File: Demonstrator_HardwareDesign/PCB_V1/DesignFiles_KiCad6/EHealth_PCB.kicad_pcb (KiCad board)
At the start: 2 copper layers, 50 x 50 mm, 24 parts

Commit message: aangepaste pcb layout
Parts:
- removed AnalogSensors: Conn_01x05, Connector_PinHeader_2.54mm:PinHeader_1x05_P2.54mm_Vertical
- removed R10, R11, R12, R5, R6, R7, R8, R9: R, Resistor_SMD:R_0805_2012Metric_Pad1.20x1.40mm_HandSolder
- added J1: Conn_01x06, Connector_PinHeader_2.54mm:PinHeader_2x04_P2.54mm_Vertical, F.Cu at (215.2, 92.2)
- added R16: R, Resistor_SMD:R_0805_2012Metric_Pad1.20x1.40mm_HandSolder, F.Cu at (208.0, 99.3)
- added R17: R, Resistor_SMD:R_0805_2012Metric_Pad1.20x1.40mm_HandSolder, F.Cu at (208.1, 94.2)
- added R21: R, Resistor_SMD:R_0805_2012Metric_Pad1.20x1.40mm_HandSolder, F.Cu at (210.0, 97.0)
- added R22: R, Resistor_SMD:R_0805_2012Metric_Pad1.20x1.40mm_HandSolder, F.Cu at (210.1, 91.9)
- J3-MagneticInterconnect1: renamed from MagneticInterconnect; footprint Connector_JST:JST_VH_B8P-VH-B_1x08_P3.96mm_Vertical -> Connector_JST:JST_VH_B4P-VH-B_1x04_P3.96mm_Vertical
- J4-OffTheShelf-Digital1: renamed from Digital; footprint Connector_PinSocket_2.54mm:PinSocket_2x06_P2.54mm_Vertical -> Connector_PinSocket_2.54mm:PinSocket_2x04_P2.54mm_Vertical
- moved R1 10.8 mm to (193.0, 103.8)
- moved R18 8.32 mm to (225.5, 102.2), turned to 0 degrees
- moved R20 8.32 mm to (225.5, 91.9), turned to 0 degrees
- moved R19 8.31 mm to (225.5, 97.0), turned to 0 degrees
- moved R14 7.96 mm to (223.5, 99.3)
- moved R13 7.95 mm to (223.5, 104.3)
- moved R15 7.95 mm to (223.5, 94.2)
- renumbered Power to J5-Power1, R16 to R18, R17 to R19, R18 to R20
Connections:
- LOLIN_C3_PICO1 pad 15: Net-(J1-AnalogSensors1-Pin_5) -> unconnected-(LOLIN_C3_PICO1-5_-_A5-Pad15)
- R13 pad 1: Net-(J1-AnalogSensors1-Pin_5) -> /SPI_MOSI
- R18 pad 1: Net-(J1-AnalogSensors1-Pin_5) -> /SPI_MOSI
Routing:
- net /SPI_CS: track 73.5 -> 0.00 mm, vias 2 -> 0
- net /SPI_MISO: track 82.2 -> 18.5 mm, vias 1 -> 0
- net Net-(J1-AnalogSensors1-Pin_5): track 34.4 -> 0.00 mm
- net +3.3V: track 140.5 -> 172.1 mm, vias 3 -> 6
- net /SPI_SCK: track 68.1 -> 40.6 mm, vias 1 -> 0
- net /SPI_MOSI: track 67.0 -> 44.6 mm
- net GND: track 47.4 -> 27.6 mm, vias 10 -> 8
- net Net-(J4-OffTheShelf-Digital1-Pin_5): track 23.5 -> 12.6 mm
- net /GPIO21_TX: track 55.4 -> 49.9 mm
- net /GPIO20_RX: track 52.1 -> 47.2 mm
- net /GPIO4_LED: track 66.5 -> 62.2 mm, vias 2 -> 0
- net Net-(J1-Pin_4): track 47.2 -> 43.6 mm
- net Net-(J1-Pin_5): track 51.8 -> 52.6 mm, vias 0 -> 2
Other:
- outline, holes or cut-outs redrawn
- board text added: "GPIO0"
- board text added: "GPIO1"
- board text added: "GPIO2"
- board text added: "IMO-IMOMEC"
- board text removed: "CS"
- board text removed: "CS SCK"
- board text removed: "GPIO5"
- board text removed: "MISO"
- board text removed: "MOSI"
- board text removed: "MOSI MISO"
- board text removed: "Optional"
- board text removed: "SCK"
- board text removed: "SPI P_Up/Down"

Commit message: aangepaste layout
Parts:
- removed R1, R18, R19, R20, R21, R22: R, Resistor_SMD:R_0805_2012Metric_Pad1.20x1.40mm_HandSolder
- J1: footprint Connector_PinHeader_2.54mm:PinHeader_2x04_P2.54mm_Vertical -> Connector_PinHeader_2.54mm:PinHeader_2x05_P2.54mm_Vertical
- moved J4-OffTheShelf-Digital1 25.3 mm to (183.8, 76.2), turned to 0 degrees
- moved J1 15.4 mm to (226.3, 103.0), turned to 180 degrees
- moved R13 13.1 mm to (216.5, 93.2)
- moved R17 11.8 mm to (216.5, 102.5)
- moved R16 8.52 mm to (216.5, 100.1)
- moved R15 7.90 mm to (216.5, 97.8)
- moved R14 7.89 mm to (216.5, 95.6)
- renumbered J3-MagneticInterconnect1 to MagneticInterconnect1
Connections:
- J1 pad 1: +3.3V -> GND
- J1 pad 2: GND -> Net-(J1-Pin_2)
- J1 pad 3: /SPI_SCK -> GND
- J1 pad 5: Net-(J1-Pin_5) -> GND
- J1 pad 6: /SPI_MOSI -> Net-(J1-Pin_6)
- J1 pad 7: /SPI_MISO -> GND
- J1 pad 8: GND -> Net-(J1-Pin_8)
- J4-OffTheShelf-Digital1 pad 5: Net-(J4-OffTheShelf-Digital1-Pin_5) -> /SPI_CS
- LOLIN_C3_PICO1 pad 10: Net-(J1-Pin_5) -> Net-(J1-Pin_8)
- LOLIN_C3_PICO1 pad 11: Net-(J1-Pin_4) -> Net-(J1-Pin_6)
- LOLIN_C3_PICO1 pad 12: /SPI_SCK -> Net-(J1-Pin_4)
- LOLIN_C3_PICO1 pad 13: /SPI_MISO -> Net-(J1-Pin_2)
- LOLIN_C3_PICO1 pad 14: /SPI_MOSI -> Net-(J1-Pin_10)
- MagneticInterconnect1 pad 1: +3.3V -> Vdd
- R13 pad 1: /SPI_MOSI -> Net-(J1-Pin_10)
- R14 pad 1: Net-(J1-Pin_5) -> Net-(J1-Pin_8)
- R15 pad 1: Net-(J1-Pin_4) -> Net-(J1-Pin_6)
- R16 pad 1: /SPI_SCK -> Net-(J1-Pin_4)
- R17 pad 1: /SPI_MISO -> Net-(J1-Pin_2)
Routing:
- net Net-(J1-Pin_5): track 52.6 -> 0.00 mm, vias 2 -> 0
- net Net-(J1-Pin_8): track 0.00 -> 52.3 mm, vias 0 -> 1
- net +3.3V: track 172.1 -> 120.3 mm, vias 6 -> 2
- net /SPI_CS: track 0.00 -> 49.1 mm, vias 0 -> 2
- net Net-(J1-Pin_6): track 0.00 -> 47.1 mm, vias 0 -> 1
- net /SPI_MOSI: track 44.6 -> 0.00 mm, vias 1 -> 0
- net /SPI_SCK: track 40.6 -> 0.00 mm
- net Net-(J1-Pin_2): track 0.00 -> 37.7 mm
- net /SCL: track 79.2 -> 54.2 mm
- net Net-(J1-Pin_10): track 0.00 -> 22.2 mm, vias 0 -> 1
- net /SPI_MISO: track 18.5 -> 0.00 mm
- net Net-(J4-OffTheShelf-Digital1-Pin_5): track 12.6 -> 0.00 mm
- net GND: track 27.6 -> 16.4 mm, vias 8 -> 2
- net /GPIO20_RX: track 47.2 -> 41.0 mm
- net /GPIO21_TX: track 49.9 -> 46.3 mm, vias 0 -> 2
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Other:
- outline, holes or cut-outs redrawn
- board text added: "Analog sensors"
- board text added: "Buck Convertor"
- board text removed: "Analog sensors: Mandatory Resistor deviders"
- board text removed: "Connect sensor to 3.3V or GND externally!"
- board text removed: "IMO-IMOMEC"
- board text removed: "Optional 0805 to ground"

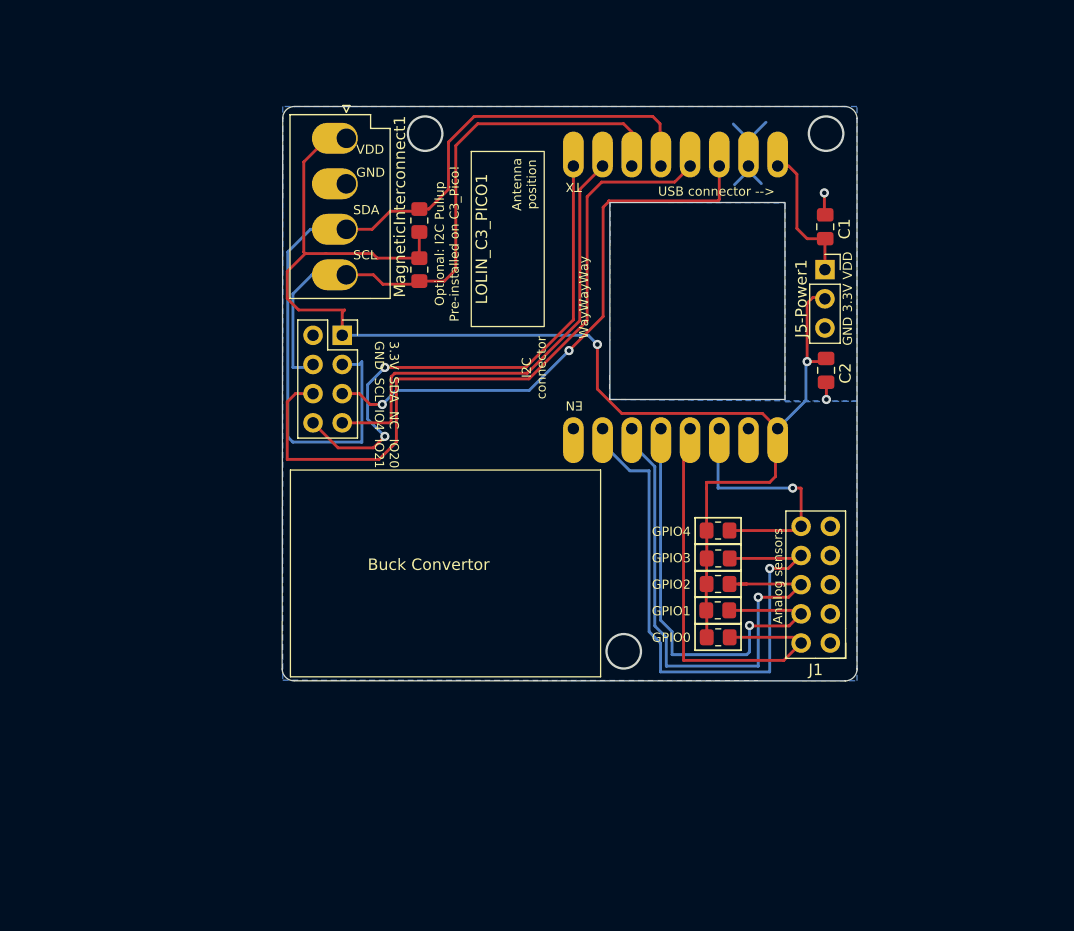
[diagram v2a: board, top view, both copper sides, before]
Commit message: layout met buck en mult chip
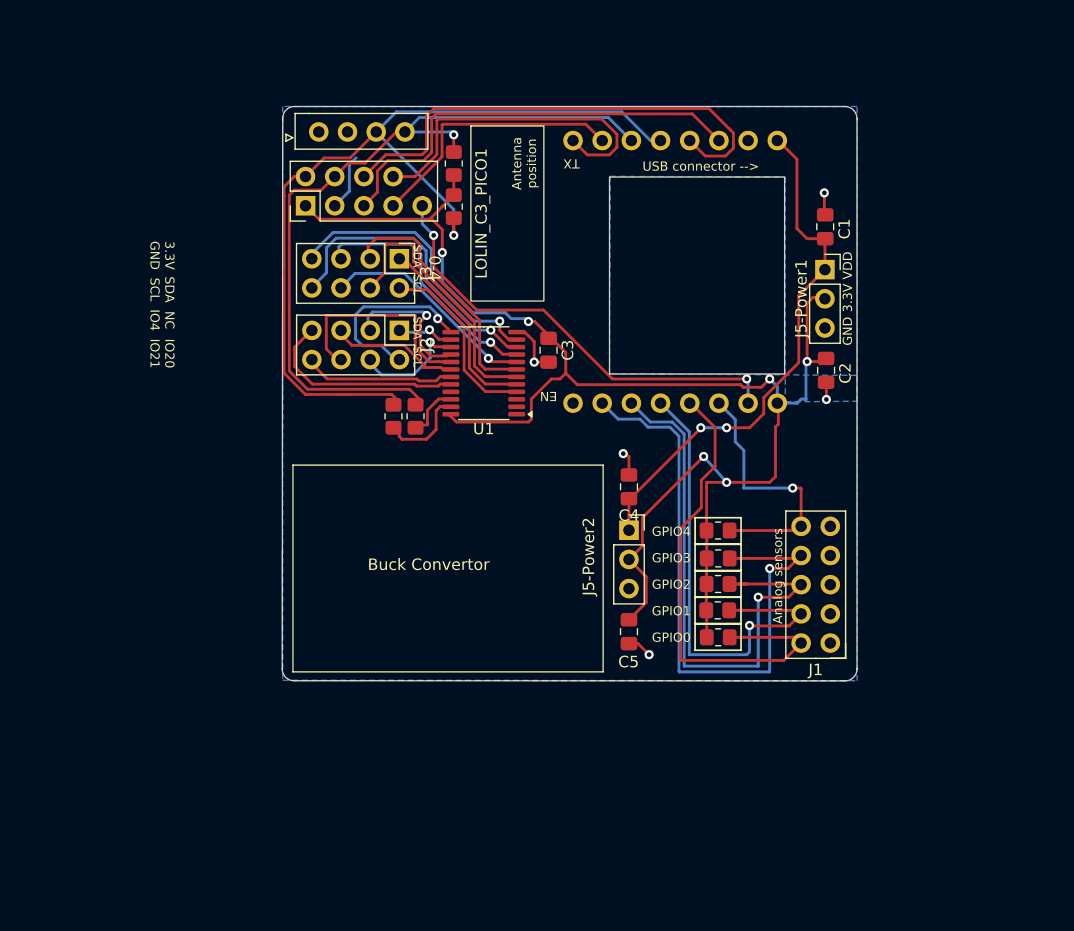
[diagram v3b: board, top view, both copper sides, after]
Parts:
- added C3: C_Small, Capacitor_SMD:C_0805_2012Metric_Pad1.18x1.45mm_HandSolder, F.Cu at (201.8, 77.5)
- added C4: C_Small, Capacitor_SMD:C_0805_2012Metric_Pad1.18x1.45mm_HandSolder, F.Cu at (208.8, 89.4)
- added C5: C_Small, Capacitor_SMD:C_0805_2012Metric_Pad1.18x1.45mm_HandSolder, F.Cu at (208.8, 102.0)
- added J2: Conn_01x06, Connector_PinHeader_2.54mm:PinHeader_2x04_P2.54mm_Vertical, F.Cu at (188.8, 75.8)
- added J3: Conn_01x06, Connector_PinHeader_2.54mm:PinHeader_2x04_P2.54mm_Vertical, F.Cu at (188.8, 69.5)
- added J5-Power2: Conn_01x03, Connector_PinSocket_2.54mm:PinSocket_1x03_P2.54mm_Vertical, F.Cu at (208.8, 93.2)
- added R1: R, Resistor_SMD:R_0805_2012Metric_Pad1.20x1.40mm_HandSolder, F.Cu at (190.2, 83.2)
- added R4: R, Resistor_SMD:R_0805_2012Metric_Pad1.20x1.40mm_HandSolder, F.Cu at (188.2, 83.2)
- added U1: TCA9548APWR, Package_SO:TSSOP-24_4.4x7.8mm_P0.65mm, F.Cu at (196.1, 79.5)
- J4-OffTheShelf-Digital1: footprint Connector_PinSocket_2.54mm:PinSocket_2x04_P2.54mm_Vertical -> Connector_PinHeader_2.54mm:PinHeader_2x05_P2.54mm_Vertical
- moved J4-OffTheShelf-Digital1 11.7 mm to (180.6, 64.9), turned to 90 degrees
- moved R3 9.71 mm to (193.5, 61.2), turned to -90 degrees
- moved R2 3.23 mm to (193.5, 65.0), turned to 90 degrees
- moved J3-MagneticInterconnect1 2.40 mm to (181.8, 59.0), turned to 0 degrees
- moved LOLIN_C3_PICO1 2.22 mm to (214.0, 69.4)
- renumbered MagneticInterconnect1 to J3-MagneticInterconnect1
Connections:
- J4-OffTheShelf-Digital1 pad 2: GND -> /SDA
- J4-OffTheShelf-Digital1 pad 3: /SDA -> GND
- LOLIN_C3_PICO1 pad 15: unconnected-(LOLIN_C3_PICO1-5_-_A5-Pad15) -> /A5
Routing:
- net /A5: track 0.00 -> 39.2 mm, vias 0 -> 2
- net VDD: track 12.2 -> 46.1 mm, vias 0 -> 2
- net Net-(J3-Pin_8): track 0.00 -> 26.4 mm, vias 0 -> 1
- net Net-(J3-Pin_7): track 0.00 -> 24.9 mm, vias 0 -> 1
- net Net-(J3-Pin_4): track 0.00 -> 23.6 mm
- net Net-(J3-Pin_3): track 0.00 -> 22.0 mm
- net Net-(J3-Pin_5): track 0.00 -> 22.0 mm, vias 0 -> 1
- net /GPIO4_LED: track 62.8 -> 43.2 mm
- net Net-(J3-Pin_6): track 0.00 -> 19.2 mm, vias 0 -> 1
- net Net-(J2-Pin_6): track 0.00 -> 18.4 mm
- net Net-(J2-Pin_7): track 0.00 -> 17.7 mm
- net Net-(J3-Pin_1): track 0.00 -> 16.8 mm
- net /GPIO21_TX: track 46.3 -> 29.6 mm, vias 2 -> 0
- net /GPIO20_RX: track 41.0 -> 24.3 mm
- net Net-(J2-Pin_2): track 0.00 -> 16.1 mm, vias 0 -> 1
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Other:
- outline, holes or cut-outs redrawn
- board text added: "0-4"
- board text removed: "I2C connector"
- board text removed: "Optional: I2C Pullup Pre-installed on C3_Pico!"
- board text removed: "WayWayWay"

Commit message: schema met mult chip en buck convertor
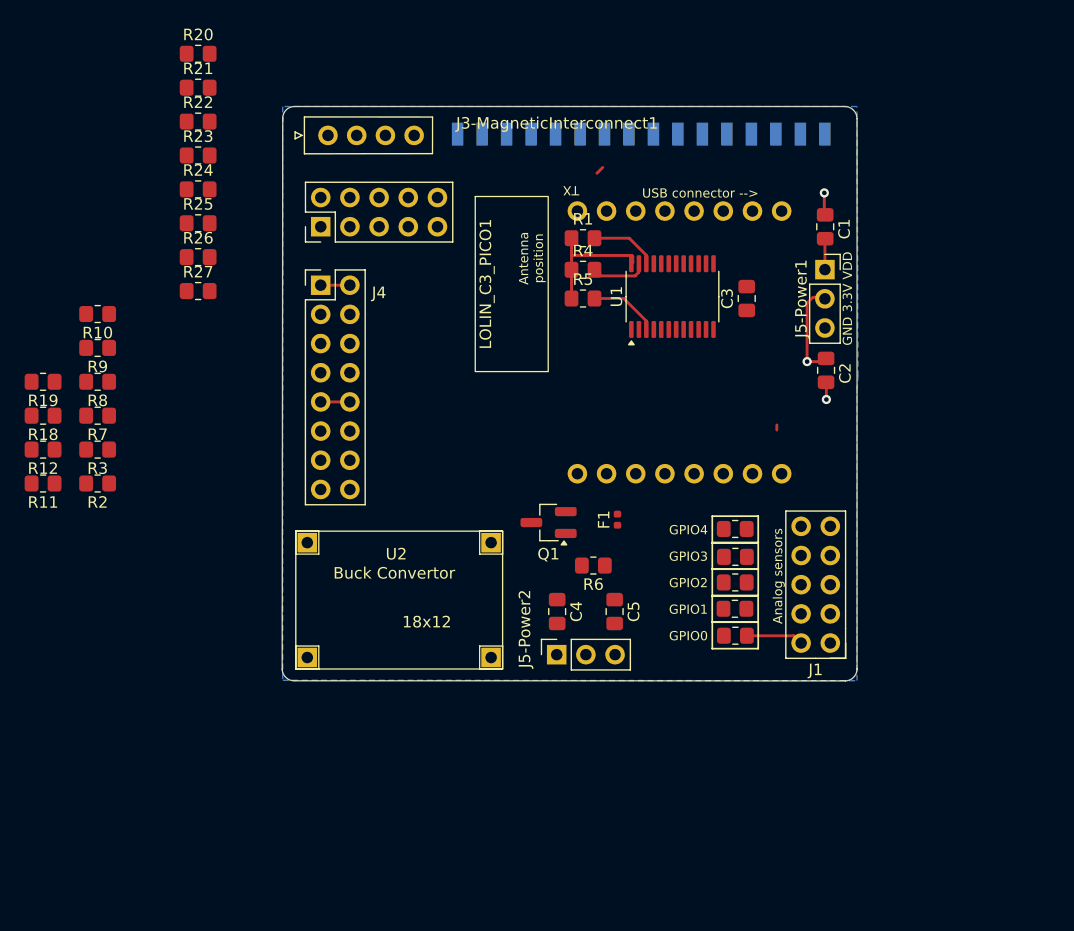
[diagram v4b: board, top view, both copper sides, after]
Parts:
- removed J3: Conn_01x06, Connector_PinHeader_2.54mm:PinHeader_2x04_P2.54mm_Vertical
- added F1: Fuse, Fuse:Fuse_0402_1005Metric, F.Cu at (207.8, 92.2)
- added J4: Conn_01x06, Connector_PinHeader_2.54mm:PinHeader_2x08_P2.54mm_Vertical, F.Cu at (181.9, 71.8)
- added Q1: PMOS, Package_TO_SOT_SMD:SOT-23_Handsoldering, F.Cu at (201.8, 92.5)
- added R10: R, Resistor_SMD:R_0805_2012Metric_Pad1.20x1.40mm_HandSolder, F.Cu at (162.5, 74.3)
- added R11: R, Resistor_SMD:R_0805_2012Metric_Pad1.20x1.40mm_HandSolder, F.Cu at (157.8, 89.1)
- added R12: R, Resistor_SMD:R_0805_2012Metric_Pad1.20x1.40mm_HandSolder, F.Cu at (157.8, 86.2)
- added R18: R, Resistor_SMD:R_0805_2012Metric_Pad1.20x1.40mm_HandSolder, F.Cu at (157.8, 83.2)
- added R19: R, Resistor_SMD:R_0805_2012Metric_Pad1.20x1.40mm_HandSolder, F.Cu at (157.8, 80.2)
- added R20: R, Resistor_SMD:R_0805_2012Metric_Pad1.20x1.40mm_HandSolder, F.Cu at (171.2, 51.7)
- added R21: R, Resistor_SMD:R_0805_2012Metric_Pad1.20x1.40mm_HandSolder, F.Cu at (171.2, 54.6)
- added R22: R, Resistor_SMD:R_0805_2012Metric_Pad1.20x1.40mm_HandSolder, F.Cu at (171.2, 57.6)
- added R23: R, Resistor_SMD:R_0805_2012Metric_Pad1.20x1.40mm_HandSolder, F.Cu at (171.2, 60.5)
- added R24: R, Resistor_SMD:R_0805_2012Metric_Pad1.20x1.40mm_HandSolder, F.Cu at (171.2, 63.5)
- added R25: R, Resistor_SMD:R_0805_2012Metric_Pad1.20x1.40mm_HandSolder, F.Cu at (171.2, 66.5)
- added R26: R, Resistor_SMD:R_0805_2012Metric_Pad1.20x1.40mm_HandSolder, F.Cu at (171.2, 69.4)
- added R27: R, Resistor_SMD:R_0805_2012Metric_Pad1.20x1.40mm_HandSolder, F.Cu at (171.2, 72.3)
- added R5: R, Resistor_SMD:R_0805_2012Metric_Pad1.20x1.40mm_HandSolder, F.Cu at (204.8, 73.0)
- added R6: R, Resistor_SMD:R_0805_2012Metric_Pad1.20x1.40mm_HandSolder, F.Cu at (205.7, 96.2)
- added R7: R, Resistor_SMD:R_0805_2012Metric_Pad1.20x1.40mm_HandSolder, F.Cu at (162.5, 83.2)
- added R8: R, Resistor_SMD:R_0805_2012Metric_Pad1.20x1.40mm_HandSolder, F.Cu at (162.5, 80.2)
- added R9: R, Resistor_SMD:R_0805_2012Metric_Pad1.20x1.40mm_HandSolder, F.Cu at (162.5, 77.3)
- added U2: DEBO DCDC DOWN 4, DEBO DCDC DOWN 4:DEBO DCDC DOWN 4, F.Cu at (188.8, 97.2)
- J2: footprint Connector_PinHeader_2.54mm:PinHeader_2x04_P2.54mm_Vertical -> Connector_PinHeader_2.54mm:PinHeader_1x16_P2.54mm_Vertical; moved to B.Cu
- moved J2 45.4 mm to (230.8, 58.7), turned to 90 degrees
- moved R3 39.8 mm to (162.5, 86.2), turned to 180 degrees
- moved R2 39.3 mm to (162.5, 89.1), turned to 180 degrees
- moved R1 21.3 mm to (204.8, 67.8), turned to 0 degrees
- moved R4 20.9 mm to (204.8, 70.5), turned to 0 degrees
- moved C3 17.8 mm to (219.0, 73.0), turned to 90 degrees
- moved U1 17.7 mm to (212.5, 72.8), turned to 90 degrees
- moved C4 12.5 mm to (202.5, 100.2)
- moved J5-Power2 12.5 mm to (202.5, 104.0), turned to 90 degrees
- moved LOLIN_C3_PICO1 6.15 mm to (214.4, 75.5)
- moved J4-OffTheShelf-Digital1 2.25 mm to (181.9, 66.8)
- moved C5 2.15 mm to (207.5, 100.2), turned to -90 degrees
- moved R13 1.50 mm to (218.0, 93.1)
- moved R14 1.50 mm to (218.0, 95.5)
- moved R15 1.50 mm to (218.0, 97.7)
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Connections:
- J2 pad 1: Net-(J2-Pin_1) -> +3.3V
- J2 pad 2: Net-(J2-Pin_2) -> +3.3V
- J2 pad 3: Net-(J2-Pin_3) -> GND
- J2 pad 4: Net-(J2-Pin_4) -> GND
- J3-MagneticInterconnect1 pad 1: Vdd -> VDD_12V
- J3-MagneticInterconnect1 pad 2: GND -> GND_12V
- J4-OffTheShelf-Digital1 pad 1: +3.3V -> /A5
- J4-OffTheShelf-Digital1 pad 2: /SDA -> +3.3V
- J4-OffTheShelf-Digital1 pad 3: GND -> /SPI_CS
- J4-OffTheShelf-Digital1 pad 4: /SCL -> GND
- J4-OffTheShelf-Digital1 pad 5: /SPI_CS -> /GPIO4_LED
- J4-OffTheShelf-Digital1 pad 6: /GPIO4_LED -> /SDA
- J4-OffTheShelf-Digital1 pad 8: /GPIO21_TX -> /SCL
- J4-OffTheShelf-Digital1 pad 9: /A5 -> /GPIO21_TX
- R1 pad 1: Net-(U1-SCL) -> +3.3V
- R4 pad 1: /SDA -> +3.3V
- R4 pad 2: Net-(U1-SDA) -> /SDA
- U1 pad 13: Net-(J2-Pin_2) -> Net-(J2-Pin_7)
- U1 pad 14: Net-(J2-Pin_1) -> Net-(J2-Pin_5)
- U1 pad 15: Net-(J2-Pin_4) -> Net-(J2-Pin_8)
- U1 pad 16: Net-(J2-Pin_3) -> Net-(J2-Pin_6)
- U1 pad 17: Net-(J2-Pin_6) -> Net-(J2-Pin_15)
- U1 pad 18: Net-(J2-Pin_5) -> Net-(J2-Pin_13)
- U1 pad 19: Net-(J2-Pin_8) -> Net-(J2-Pin_16)
- U1 pad 20: Net-(J2-Pin_7) -> Net-(J2-Pin_14)
- U1 pad 22: Net-(U1-SCL) -> /SCL
- U1 pad 23: Net-(U1-SDA) -> /SDA
- U1 pad 3: unconnected-(U1-~{RESET}-Pad3) -> Net-(U1-~{RESET})
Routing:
- net +3.3V: track 134.4 -> 25.6 mm, vias 6 -> 1
- net /SDA: track 78.1 -> 4.95 mm, vias 1 -> 0
- net /SCL: track 67.3 -> 5.86 mm, vias 1 -> 0
- net Net-(J1-Pin_8): track 54.8 -> 0.00 mm, vias 1 -> 0
- net Net-(J1-Pin_6): track 49.5 -> 0.09 mm, vias 1 -> 0
- net VDD: track 46.1 -> 2.70 mm, vias 2 -> 0
- net /GPIO4_LED: track 43.2 -> 0.00 mm
- net Net-(J1-Pin_4): track 42.1 -> 0.43 mm, vias 1 -> 0
- net /A5: track 39.2 -> 0.00 mm, vias 2 -> 0
- net /SPI_CS: track 38.0 -> 0.00 mm
- net Net-(J1-Pin_2): track 42.0 -> 4.99 mm
- net /GPIO21_TX: track 29.6 -> 0.00 mm
- net Net-(J4-Pin_16): track 26.4 -> 0.00 mm, vias 1 -> 0
- net Net-(J4-Pin_14): track 24.9 -> 0.00 mm, vias 1 -> 0
- net /GPIO20_RX: track 24.3 -> 0.72 mm
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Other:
- board text added: "18x12"
- board text removed: "0-4"
- board text removed: "3.3V GND"
- board text removed: "EN"
- board text removed: "IO20 IO21"
- board text removed: "NC IO4"
- board text removed: "SCL"
- board text removed: "SDA"
- board text removed: "SDA SCL"

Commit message: up to date
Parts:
- moved R27 52.2 mm to (222.1, 84.0), turned to 90 degrees
- moved R26 50.1 mm to (219.2, 84.0), turned to 90 degrees
- moved R25 48.3 mm to (216.2, 84.0), turned to 90 degrees
- moved R24 46.7 mm to (213.2, 84.0), turned to 90 degrees
- moved R23 45.6 mm to (210.3, 84.0), turned to 90 degrees
- moved R22 44.7 mm to (207.3, 84.0), turned to 90 degrees
- moved R21 44.3 mm to (204.4, 84.0), turned to 90 degrees
- moved R20 44.2 mm to (201.4, 84.0), turned to 90 degrees
- moved R11 36.3 mm to (194.0, 89.7)
- moved R12 36.3 mm to (194.0, 86.7)
- moved R18 36.3 mm to (194.0, 83.8)
- moved R19 36.3 mm to (194.0, 80.8)
- moved R10 26.8 mm to (189.2, 74.9)
- moved R2 26.8 mm to (189.2, 89.7)
- moved R3 26.8 mm to (189.2, 86.7)
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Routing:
- net +3.3V: track 25.6 -> 14.3 mm
- net Net-(U1-~{RESET}): track 6.06 -> 0.00 mm
- net /SCL: track 5.86 -> 0.00 mm
- net Net-(J1-Pin_2): track 4.99 -> 0.00 mm
- net /SDA: track 4.95 -> 0.00 mm
- net /GPIO20_RX: track 0.72 -> 0.00 mm

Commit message: up to date
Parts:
- F1: footprint Fuse:Fuse_0402_1005Metric -> Fuse:Fuse_0805_2012Metric_Pad1.15x1.40mm_HandSolder
- Q1: footprint Package_TO_SOT_SMD:SOT-23_Handsoldering -> Package_SO:Infineon_PG-DSO-8-27_3.9x4.9mm_EP2.65x3mm
- moved R19 29.0 mm to (222.8, 84.5), turned to 90 degrees
- moved R18 26.5 mm to (220.4, 84.5), turned to 90 degrees
- moved R2 25.0 mm to (213.8, 84.5), turned to 90 degrees
- moved R12 24.3 mm to (218.2, 84.5), turned to 90 degrees
- moved R11 22.6 mm to (216.0, 84.5), turned to 90 degrees
- moved R3 22.4 mm to (211.5, 84.5), turned to -90 degrees
- moved R7 20.0 mm to (209.2, 84.5), turned to -90 degrees
- moved R8 18.1 mm to (207.0, 84.5), turned to -90 degrees
- moved R9 16.9 mm to (204.8, 84.5), turned to -90 degrees
- moved R10 16.4 mm to (202.5, 84.5), turned to -90 degrees
- moved R20 15.4 mm to (207.2, 69.8)
- moved F1 15.3 mm to (193.2, 87.2), turned to -90 degrees
- moved R21 15.1 mm to (209.2, 69.8)
- moved R22 14.8 mm to (211.3, 69.8)
- moved R23 14.6 mm to (213.4, 69.8)
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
